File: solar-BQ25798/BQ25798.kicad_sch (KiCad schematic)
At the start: 33 parts, among them U1701 BQ25798RQMR

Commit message: Getting ready for v0.3.0
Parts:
- removed C1719: 100uF 50V, Capacitor_THT:CP_Radial_D6.3mm_P2.50mm, symbol Device:C_Polarized
- TP1701, TP1702: footprint cacophony-library:TP_PAD -> cacophony-library:TP_PAD_S

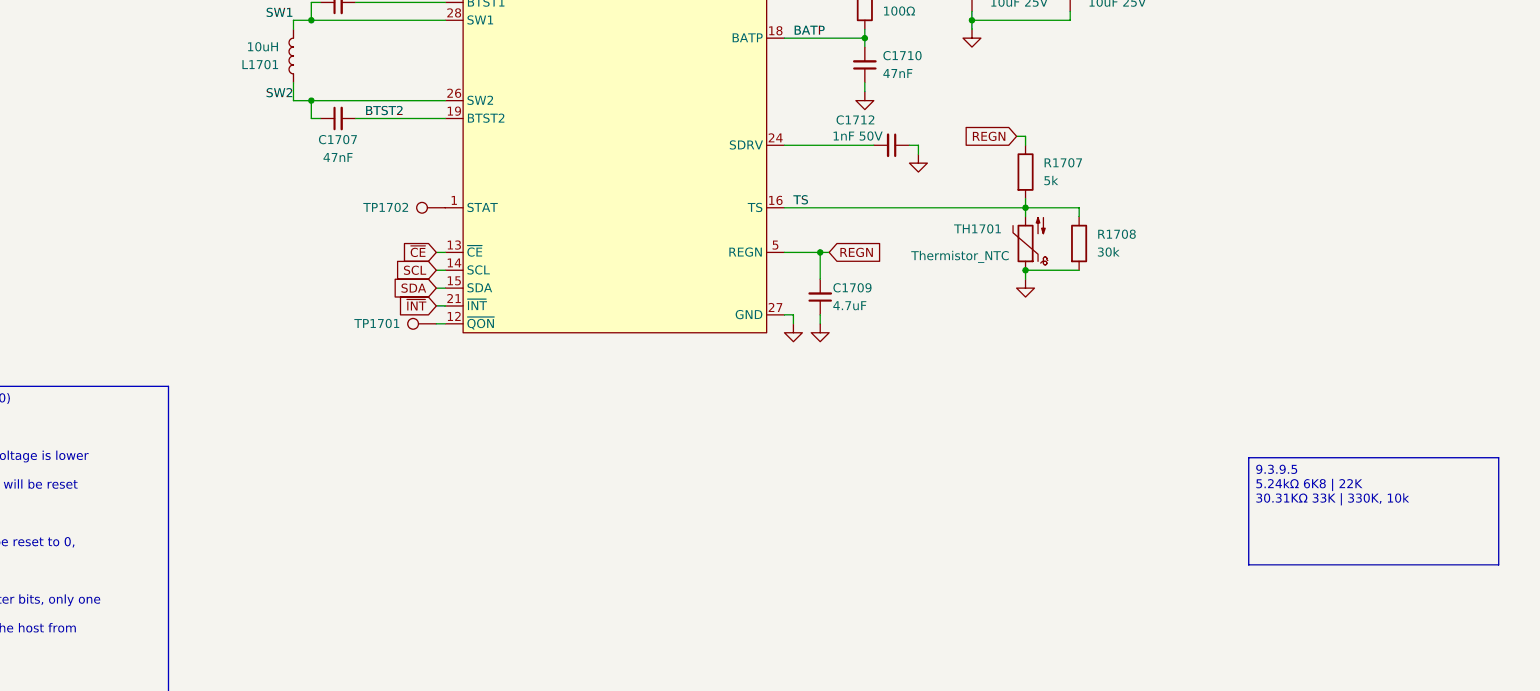
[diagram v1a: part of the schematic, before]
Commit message: Add pull up resistor for /CE and updated charger temperature range resistors
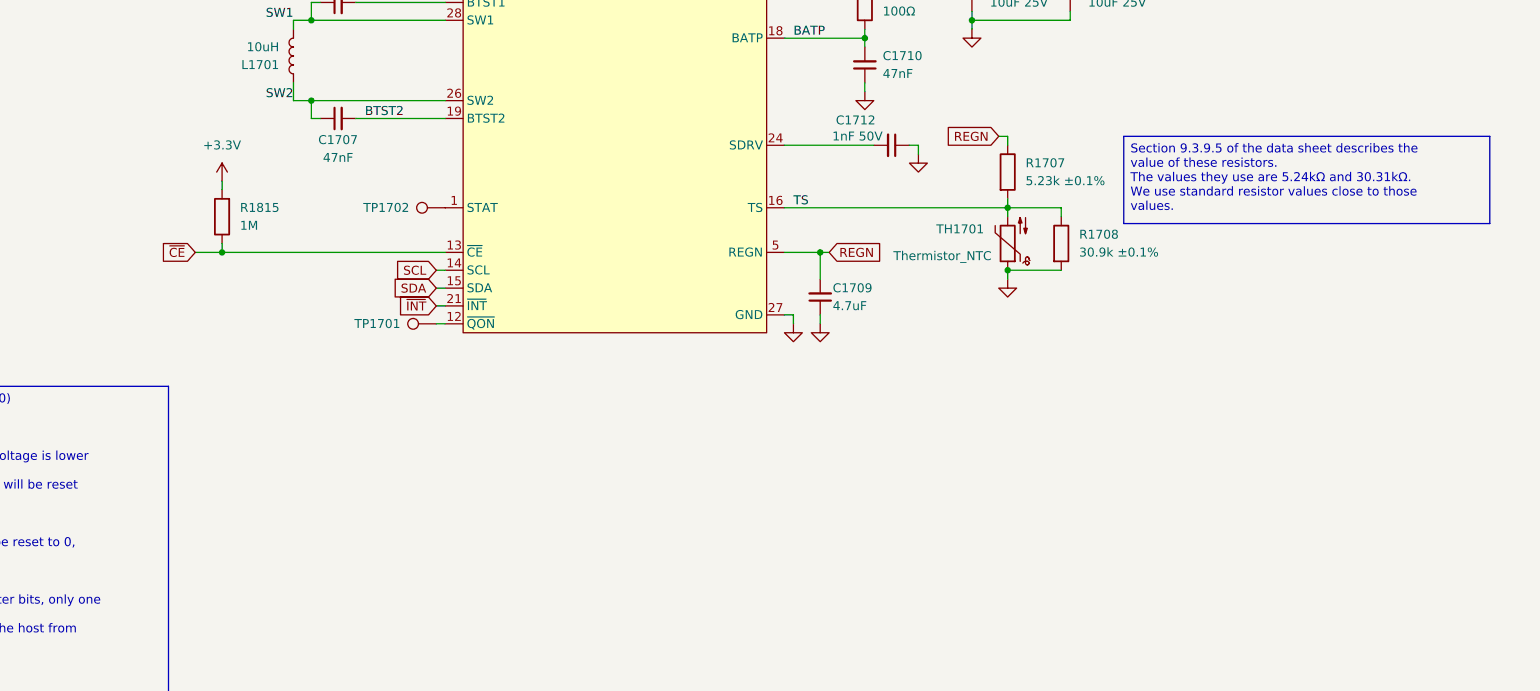
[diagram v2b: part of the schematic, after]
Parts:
- added R1815: 1M, Resistor_SMD:R_0402_1005Metric, symbol Device:R
- R1707: value 5k -> 5.23k ±0.1%; LCSC Part C5948099 -> C852857
- R1708: value 30k -> 30.9k ±0.1%; LCSC Part C25553 -> C853209
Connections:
- net ~{CE}: now also R1815.1
- new net +3.3V: R1815.2
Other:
- moved on the sheet: R1707, R1708, TH1701

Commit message: Tidy up
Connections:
- net SDRV: now reaches C1712.2, U1701.24 (SDRV)
- net STAT: now reaches TP1702.1, U1701.1 (STAT)
- net ~{QON}: now reaches TP1701.1, U1701.12 (~{QON})
- net ILIM_HIZ: now reaches R1705.1, U1701.17 (ILIM_HIZ)
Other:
- note removed: "The host can disable the OOA by setting DIS_FWD_OOA = 1"
- moved on the sheet: C1701, C1703, C1704, C1705, C1706, C1707, C1708, C1709, C1710, C1711, C1712, C1713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
